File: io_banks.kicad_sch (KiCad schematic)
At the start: 27 parts, among them J2 AUX, J3 Conn_01x02, J4 PinHeader_2x22_P1.27mm, U4 ICE40HX8K-BG121, U5 SN74LVC1T45DCKR

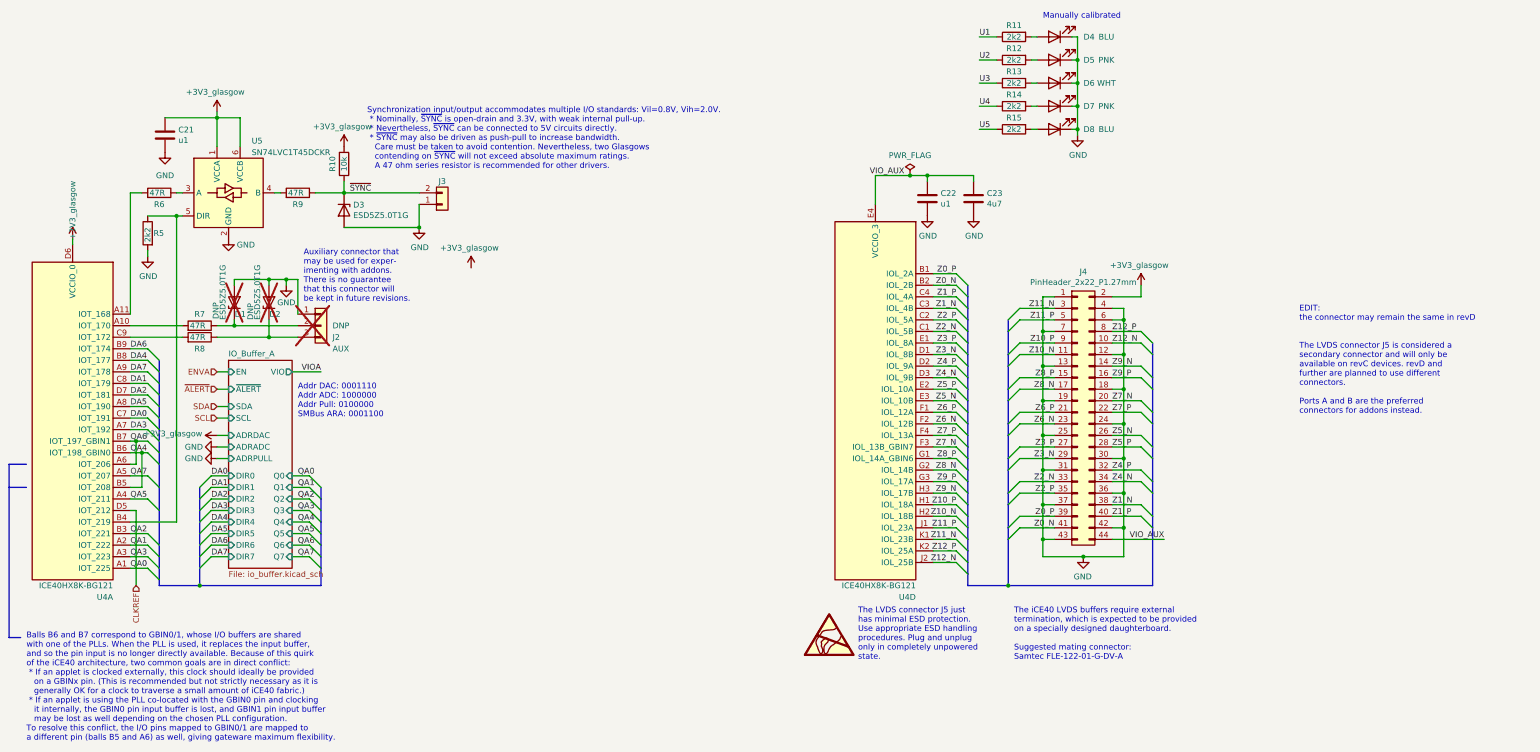
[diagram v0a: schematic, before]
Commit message: finished schematic draft and started placing components
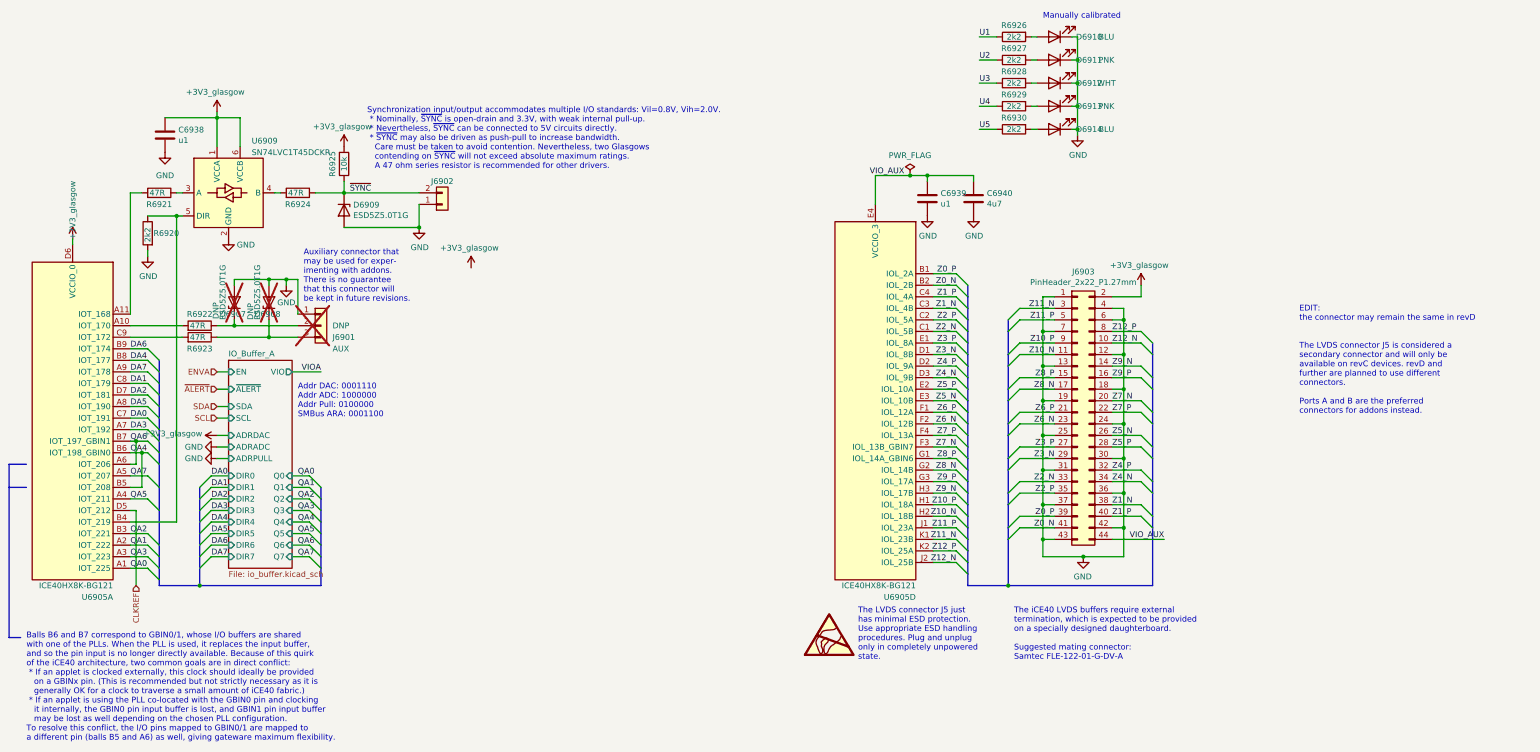
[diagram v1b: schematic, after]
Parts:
- renumbered C21 to C6938, C22 to C6939, C23 to C6940, D1 to D6907, D2 to D6908, D3 to D6909, D4 to D6910, D5 to D6911, D6 to D6912, D7 to D6913, D8 to D6914, J2 to J6901, J3 to J6902, J4 to J6903, R5 to R6920, R6 to R6921, R7 to R6922, R8 to R6923, R9 to R6924, R10 to R6925, R11 to R6926, R12 to R6927, R13 to R6928, R14 to R6929, R15 to R6930, U4 to U6905, U5 to U6909

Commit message: commit before removing duplicated glasgow
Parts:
- renumbered C6938 to C131, C6939 to C132, C6940 to C133, D6907 to D14, D6908 to D15, D6909 to D16, D6910 to D17, D6911 to D18, D6912 to D19, D6913 to D20, D6914 to D21, J6901 to J25, J6902 to J26, J6903 to J27, R6920 to R60, R6921 to R61, R6922 to R62, R6923 to R63, R6924 to R64, R6925 to R65, R6926 to R66, R6927 to R67, R6928 to R68, R6929 to R69, R6930 to R70, U6905 to U22, U6909 to U26

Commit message: some schem fixes
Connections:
- net +3V3_glasgow: now also U22.F8 (VCCIO_1)
- net U1: now also U22.G9 (IOR_128)
- net U2: now also U22.G8 (IOR_118)
- net U3: now also U22.E9 (IOR_144)
- net U4: now also U22.D9 (IOR_147)
- net U5: now also U22.E8 (IOR_146)

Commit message: more fixes, tweaks, pretty
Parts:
- added unit 2 of U22
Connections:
- net +3V3_glasgow: now also U22.F8 (VCCIO_1); no longer U22.F8 (VCCIO_1)
- net U1: now also U22.G9 (IOR_128); no longer U22.G9 (IOR_128)
- net U2: now also U22.G8 (IOR_118); no longer U22.G8 (IOR_118)
- net U3: now also U22.E9 (IOR_144); no longer U22.E9 (IOR_144)
- net U4: now also U22.D9 (IOR_147); no longer U22.D9 (IOR_147)
- net U5: now also U22.E8 (IOR_146); no longer U22.E8 (IOR_146)

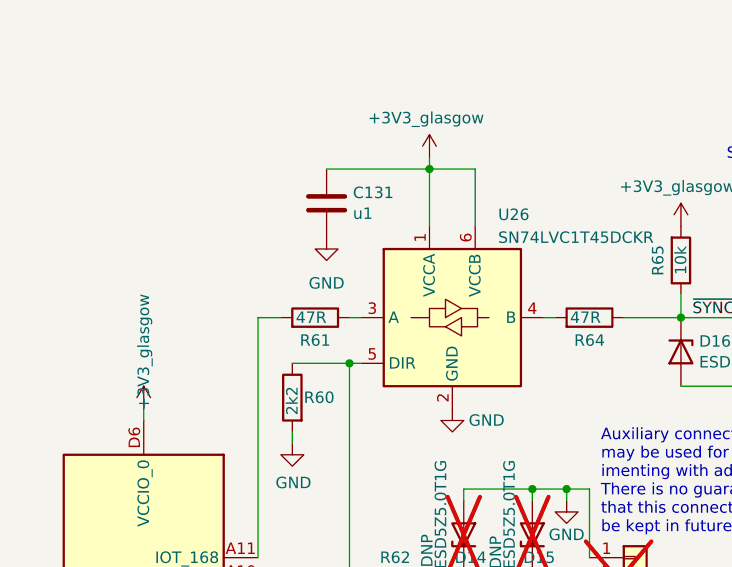
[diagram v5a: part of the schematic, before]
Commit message: added USB-C
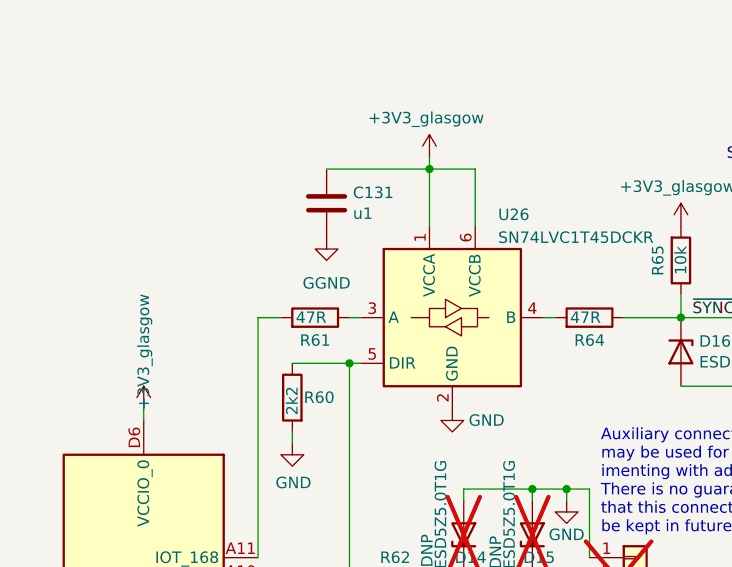
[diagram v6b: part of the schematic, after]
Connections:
- net GND: no longer C131.2
- new net GGND: C131.2
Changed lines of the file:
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@@
 			)
 		)
-		(property "Value" "GND"
+		(property "Value" "GGND"
 			(at 53.34 57.15 0)
 			(show_name no)

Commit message: added MPN to all parts by hand :'(
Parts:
- C131, C132: MPN TMK105BJ104KV-F -> C1005X7R1H104K050BE
- C133: footprint Capacitor_SMD:C_0603_1608Metric -> A_DFRobot:C_0805_2012Metric; 1b2-bom-key cap-cer-0603-4u7 -> (none); MPN LMK107BJ475KAHT -> GRM21BR61H475KE51L; Mfg Taiyo Yuden -> (none)
- R60: 1b2-bom-key res-0402-2k2 -> (none); MPN RC0402FR-132K2L -> RCS04022K20FKED; Mfg Yageo -> (none)
- R65: 1b2-bom-key res-0402-10k -> (none); MPN RC0402FR-1310KL -> RCS040210K0FKED; Mfg Yageo -> (none)
- R66, R67, R68, R69, R70: MPN RC0402FR-132K2L -> RCS04022K20FKED
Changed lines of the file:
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@@
 			)
 		)
-		(property "Datasheet" "https://www.mouser.com/datasheet/2/447/PYu-RC_Group_51_RoHS_L_10-1527934.pdf"
+		(property "Datasheet" ""
 			(at 49.53 69.85 0)
 			(hide yes)
@@
 			)
 		)
-		(property "Mfg" "Yageo"
+		(property "Mfg" ""
 			(at 312.42 134.62 0)
 			(hide yes)
@@
 			)
 		)
-		(property "MPN" "RC0402FR-132K2L"
+		(property "MPN" "RCS04022K20FKED"
 			(at 312.42 134.62 0)
 			(hide yes)
@@
 			)
 		)
-		(property "1b2-bom-key" "res-0402-2k2"
+		(property "1b2-bom-key" ""
 			(at 49.53 69.85 0)
 			(hide yes)
@@
 			)
 		)
-		(property "MPN" "RC0402FR-132K2L"
+		(property "MPN" "RCS04022K20FKED"
 			(at 262.89 -224.79 0)
 			(hide yes)
@@
 			)
 		)
-		(property "MPN" "RC0402FR-132K2L"
+		(property "MPN" "RCS04022K20FKED"
 			(at 278.13 -209.55 0)
 			(hide yes)
@@
 			)
 		)
-		(property "MPN" "RC0402FR-132K2L"
+		(property "MPN" "RCS04022K20FKED"
 			(at 283.21 -204.47 0)
 			(hide yes)
@@
 			)
 		)
-		(property "MPN" "RC0402FR-132K2L"
+		(property "MPN" "RCS04022K20FKED"
 			(at 267.97 -219.71 0)
 			(hide yes)
@@
 			)
 		)
-		(property "MPN" "RC0402FR-132K2L"
+		(property "MPN" "RCS04022K20FKED"
 			(at 273.05 -214.63 0)
 			(hide yes)
@@
 			)
 		)
-		(property "Datasheet" "https://www.mouser.com/datasheet/2/447/PYu-RC_Group_51_RoHS_L_10-1527934.pdf"
+		(property "Datasheet" ""
 			(at 92.71 54.61 0)
 			(hide yes)
@@
 			)
 		)
-		(property "Mfg" "Yageo"
+		(property "Mfg" ""
 			(at -170.18 -10.16 0)
 			(hide yes)
@@
 			)
 		)
-		(property "MPN" "RC0402FR-1310KL"
+		(property "MPN" "RCS040210K0FKED"
 			(at -170.18 -10.16 0)
 			(hide yes)
@@
 			)
 		)
-		(property "1b2-bom-key" "res-0402-10k"
+		(property "1b2-bom-key" ""
 			(at 92.71 54.61 0)
 			(hide yes)
@@
 			)
 		)
-		(property "MPN" "TMK105BJ104KV-F"
+		(property "MPN" "C1005X7R1H104K050BE"
 			(at -115.57 83.82 0)
 			(hide yes)
@@
 			)
 		)
-		(property "MPN" "TMK105BJ104KV-F"
+		(property "MPN" "C1005X7R1H104K050BE"
 			(at 52.07 97.79 0)
 			(hide yes)
@@
 			)
 		)
-		(property "Footprint" "Capacitor_SMD:C_0603_1608Metric"
+		(property "Footprint" "A_DFRobot:C_0805_2012Metric"
 			(at 232.1052 66.04 0)
 			(hide yes)
@@
 			)
 		)
-		(property "Datasheet" "https://www.mouser.com/datasheet/2/400/lcc_commercial_general_en-837201.pdf"
+		(property "Datasheet" ""
 			(at 231.14 62.23 0)
 			(hide yes)
@@
 			)
 		)
-		(property "Mfg" "Taiyo Yuden"
+		(property "Mfg" ""
 			(at -33.02 215.9 0)
 			(hide yes)
@@
 			)
 		)
-		(property "MPN" "LMK107BJ475KAHT"
+		(property "MPN" "GRM21BR61H475KE51L"
 			(at -33.02 215.9 0)
 			(hide yes)
@@
 			)
 		)
-		(property "1b2-bom-key" "cap-cer-0603-4u7"
+		(property "1b2-bom-key" ""
 			(at 231.14 62.23 0)
 			(hide yes)
